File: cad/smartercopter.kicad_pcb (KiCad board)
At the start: 2 copper layers, 37.7 x 16.8 mm, 71 parts, among them P1 CONN_5, P2 CONN_2, P3 CONN_2, P4 CONN_2, Q1 SiA910EDJ, SW1 SW_PUSH_4, U1 CC2541, U2 MPU-9250, U3 TPS73001, U4 TPS73001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

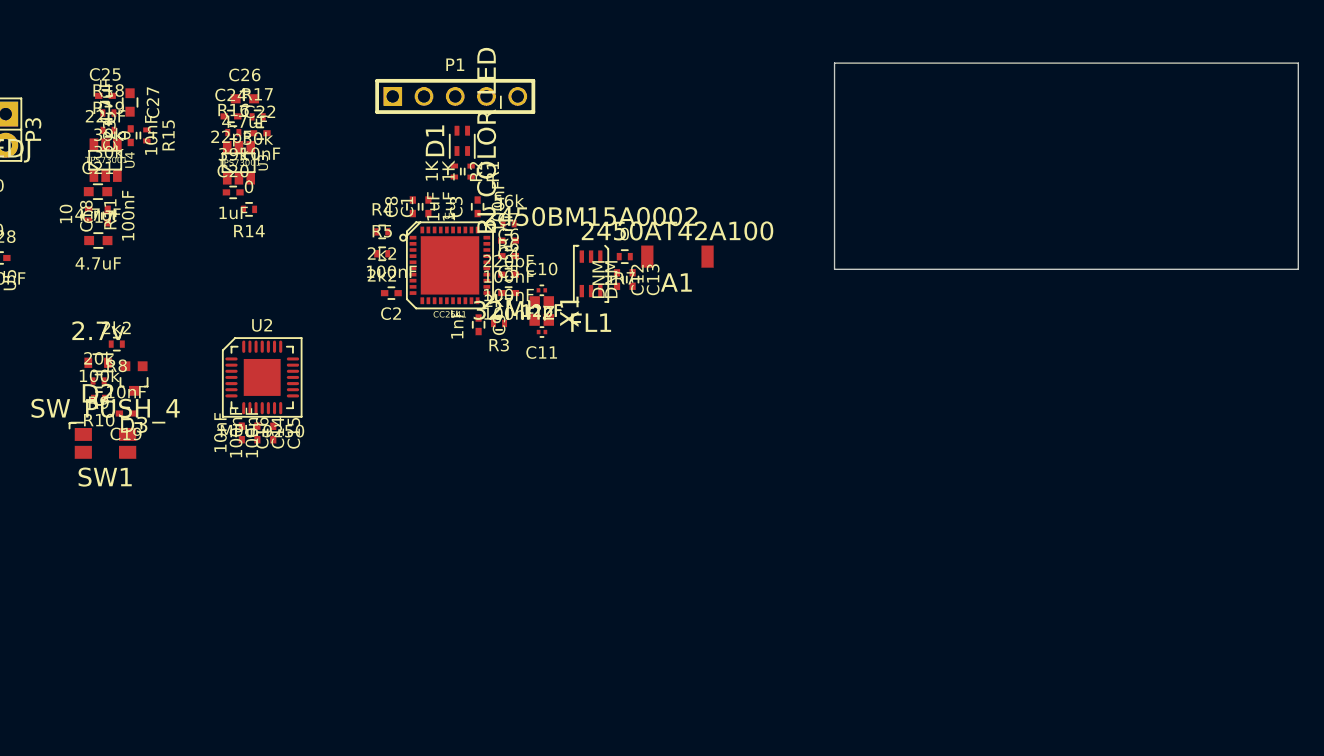
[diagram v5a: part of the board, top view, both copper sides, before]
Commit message: added board outline
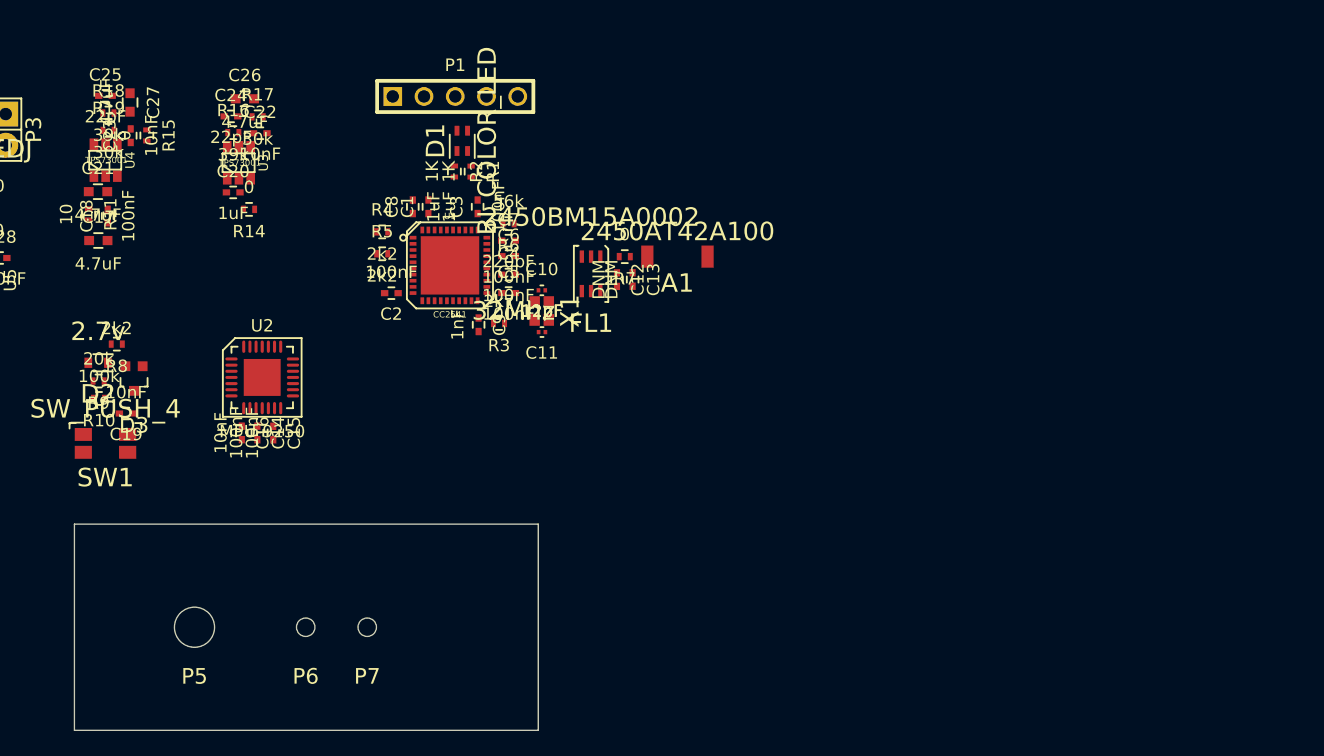
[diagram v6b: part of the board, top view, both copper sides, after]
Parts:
- added P5: CONN_01X01, Mounting_Holes:MountingHole_3mm, F.Cu at (61.1, 112.9)
- added P6: CONN_01X01, Mounting_Holes:MountingHole_3mm, F.Cu at (70.1, 112.9)
- added P7: CONN_01X01, Mounting_Holes:MountingHole_3mm, F.Cu at (75.1, 112.9)
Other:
- board text added: "Receiver"
- board text added: "Wires"
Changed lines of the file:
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@@
     (links 170)
     (no_connects 170)
-    (area 0 0 0 0)
+    (area 113.049999 66.989999 150.850001 83.850001)
     (thickness 1.6)
-    (drawings 4)
+    (drawings 6)
     (tracks 0)
     (zones 0)
-    (modules 71)
+    (modules 74)
     (nets 71)
   )
@@
     (mod_text_width 0.15)
     (pad_size 1.5 1.5)
-    (pad_drill 0.6)
+    (pad_drill 1.5)
     (pad_to_mask_clearance 0)
     (aux_axis_origin 0 0)
-    (visible_elements FFFCFF7F)
+    (visible_elements FFFEFF7F)
     (pcbplotparams
       (layerselection 0x00030_80000001)
@@
       (net 4 DGND))
   )
-  (gr_line (start 150.8 83.8) (end 113.1 83.8) (layer Edge.Cuts) (width 0.1))
-  (gr_line (start 150.8 67.04) (end 150.8 83.8) (layer Edge.Cuts) (width 0.1))
-  (gr_line (start 113.1 67.04) (end 150.8 67.04) (layer Edge.Cuts) (width 0.1))
-  (gr_line (start 113.1 83.8) (end 113.1 67.04) (layer Edge.Cuts) (width 0.1))
+  (module Mounting_Holes:MountingHole_3mm (layer F.Cu)
+    (at 61.075056 112.89367 180)
+    (descr "Mounting hole, Befestigungsbohrung, 3mm, No Annular, Kein Restring,")
+    (tags "Mounting hole, Befestigungsbohrung, 3mm, No Annular, Kein Restring,")
+    (fp_text reference P5 (at 0 -4.0005 180) (layer F.SilkS)
+      (effects (font (thickness 0.3048)))
+    )
+    (fp_text value CONN_01X01 (at 1.00076 5.00126 180) (layer F.SilkS) hide
+      (effects (font (thickness 0.3048)))
+    )
+    (fp_circle (center 0 0) (end 2.99974 0) (layer Cmts.User) (width 0.381))
+    (pad "" np_thru_hole circle (at 0 0 180) (size 3.26 3.26) (drill 3.26) (layers *.Cu *.Mask F.SilkS))
+  )
+  (module Mounting_Holes:MountingHole_3mm (layer F.Cu)
+    (at 70.115056 112.89367 180)
+    (descr "Mounting hole, Befestigungsbohrung, 3mm, No Annular, Kein Restring,")
+    (tags "Mounting hole, Befestigungsbohrung, 3mm, No Annular, Kein Restring,")
+    (fp_text reference P6 (at 0 -4.0005 180) (layer F.SilkS)
+      (effects (font (thickness 0.3048)))
+    )
+    (fp_text value CONN_01X01 (at 1.00076 5.00126 180) (layer F.SilkS) hide
+      (effects (font (thickness 0.3048)))
+    )
+    (fp_circle (center 0 0) (end 2.99974 0) (layer Cmts.User) (width 0.381))
+    (pad "" np_thru_hole circle (at 0 0 180) (size 1.5 1.5) (drill 1.5) (layers *.Cu *.Mask F.SilkS))
+  )
+  (module Mounting_Holes:MountingHole_3mm (layer F.Cu)
+    (at 75.115056 112.89367 180)
+    (descr "Mounting hole, Befestigungsbohrung, 3mm, No Annular, Kein Restring,")
+    (tags "Mounting hole, Befestigungsbohrung, 3mm, No Annular, Kein Restring,")
+    (fp_text reference P7 (at 0 -4.0005 180) (layer F.SilkS)
+      (effects (font (thickness 0.3048)))
+    )
+    (fp_text value CONN_01X01 (at 1.00076 5.00126 180) (layer F.SilkS) hide
+      (effects (font (thickness 0.3048)))
+    )
+    (fp_circle (center 0 0) (end 2.99974 0) (layer Cmts.User) (width 0.381))
+    (pad "" np_thru_hole circle (at 0 0 180) (size 1.5 1.5) (drill 1.5) (layers *.Cu *.Mask F.SilkS))
+  )
+  (gr_text Receiver (at 49.56 112.86 90) (layer Cmts.User)
+    (effects (font (size 1.5 1.5) (thickness 0.3)))
+  )
+  (gr_text Wires (at 90.88 113.06 270) (layer Cmts.User)
+    (effects (font (size 1.5 1.5) (thickness 0.3)))
+  )
+  (gr_line (start 51.315056 104.51367) (end 89.015056 104.51367) (layer Edge.Cuts) (width 0.1))
+  (gr_line (start 51.315056 121.27367) (end 51.315056 104.51367) (layer Edge.Cuts) (width 0.1))
+  (gr_line (start 89.015056 121.27367) (end 51.315056 121.27367) (layer Edge.Cuts) (width 0.1))
+  (gr_line (start 89.015056 104.51367) (end 89.015056 121.27367) (layer Edge.Cuts) (width 0.1))
 )

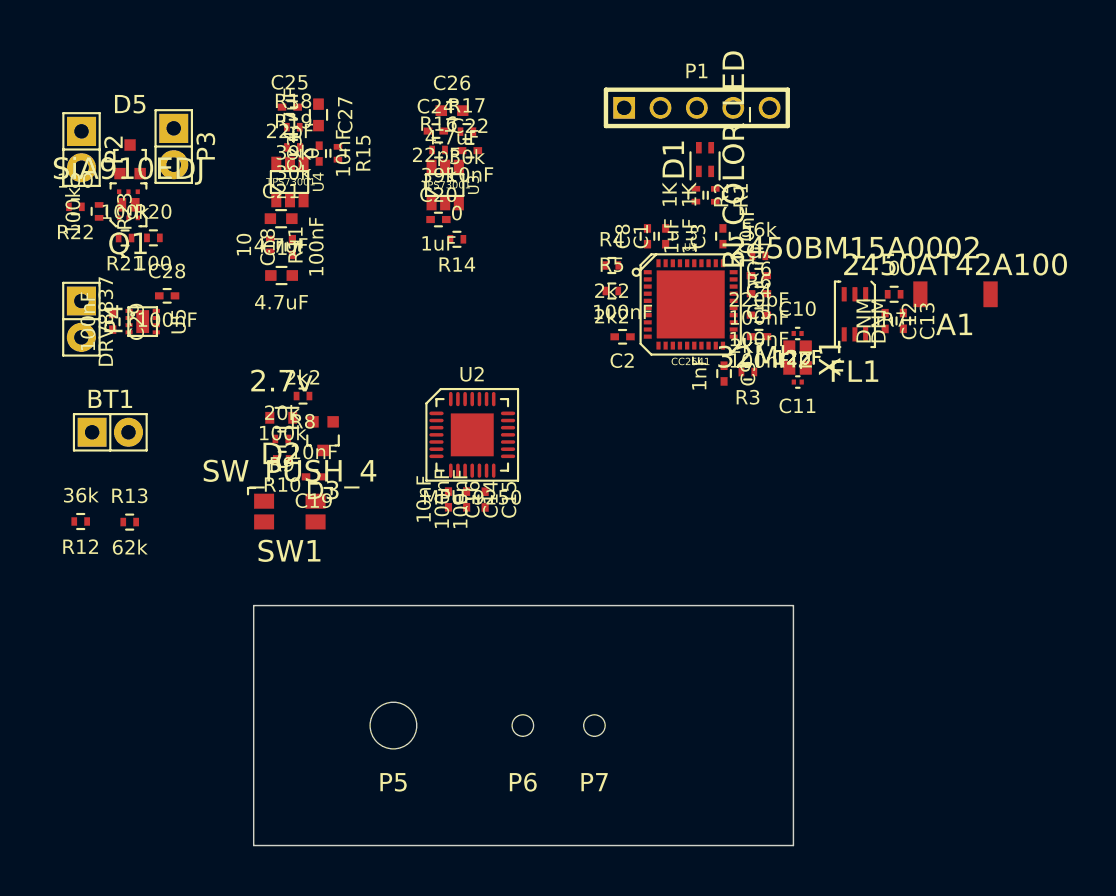
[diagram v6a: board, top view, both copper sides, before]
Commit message: made motor pads single to save space
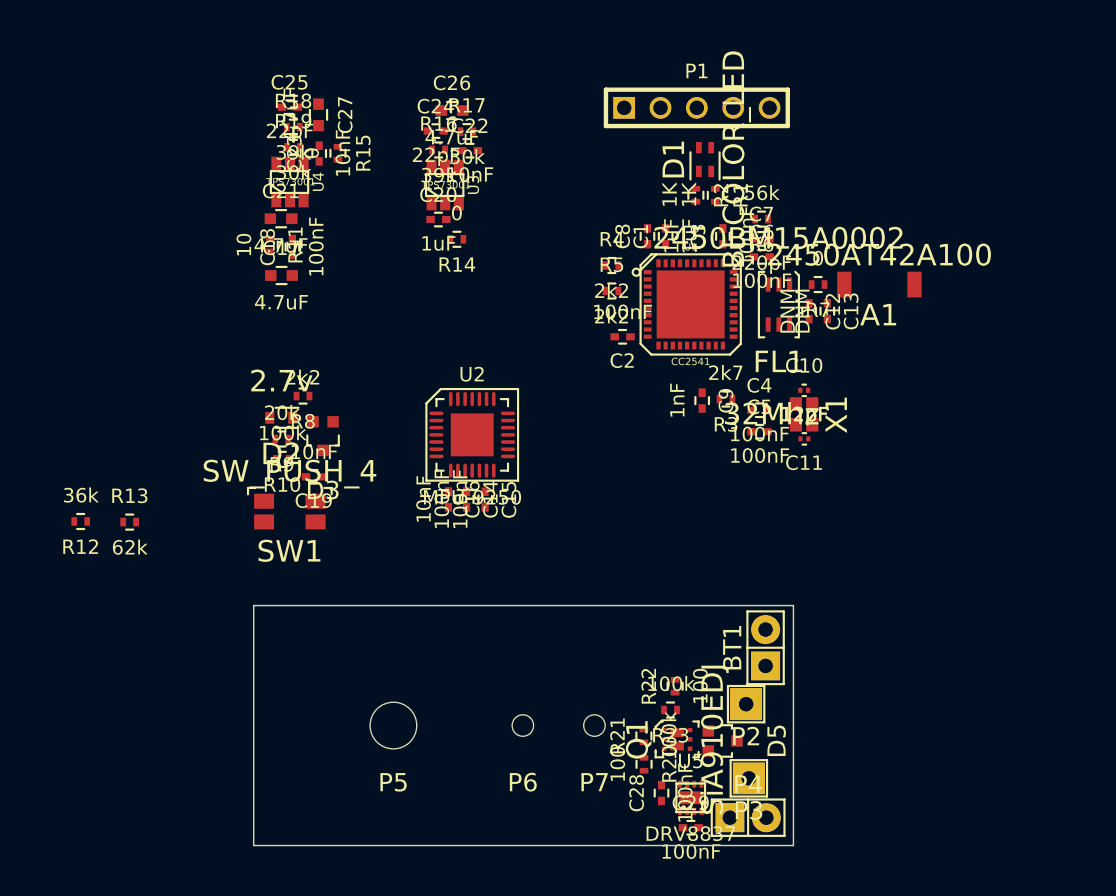
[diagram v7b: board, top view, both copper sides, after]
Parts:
- P2, P3: value CONN_2 -> CONN_01X01; footprint Pin_Headers:Pin_Header_Straight_1x02 -> Pin_Headers:Pin_Header_Straight_1x01
- moved P2 60.5 mm to (85.7, 111.4), turned to 180 degrees
- moved P3 59.7 mm to (85.9, 116.6), turned to 180 degrees
- moved P4 58.1 mm to (85.8, 119.3), turned to 0 degrees
- moved D5 58.0 mm to (84.1, 114.0), turned to 270 degrees
- moved C29 53.7 mm to (81.8, 120.0), turned to 0 degrees
- moved R22 53.6 mm to (80.8, 110.2), turned to 90 degrees
- moved Q1 53.5 mm to (80.9, 113.9), turned to 270 degrees
- moved R23 53.0 mm to (80.4, 111.8), turned to 180 degrees
- moved U5 50.7 mm to (81.8, 117.9), turned to 90 degrees
- moved R20 50.3 mm to (78.6, 115.6), turned to 270 degrees
- moved R21 50.2 mm to (78.6, 113.6), turned to 90 degrees
- moved C28 49.0 mm to (79.8, 117.6), turned to 90 degrees
- moved BT1 48.2 mm to (87.1, 107.5), turned to 90 degrees
- moved C4 6.64 mm to (86.6, 90.9)
- moved C5 6.64 mm to (86.7, 92.4)
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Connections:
- P2 pad 1: +BATT -> Net-(D5-Pad1)
- P3 pad 1: +BATT -> Net-(D5-Pad2)

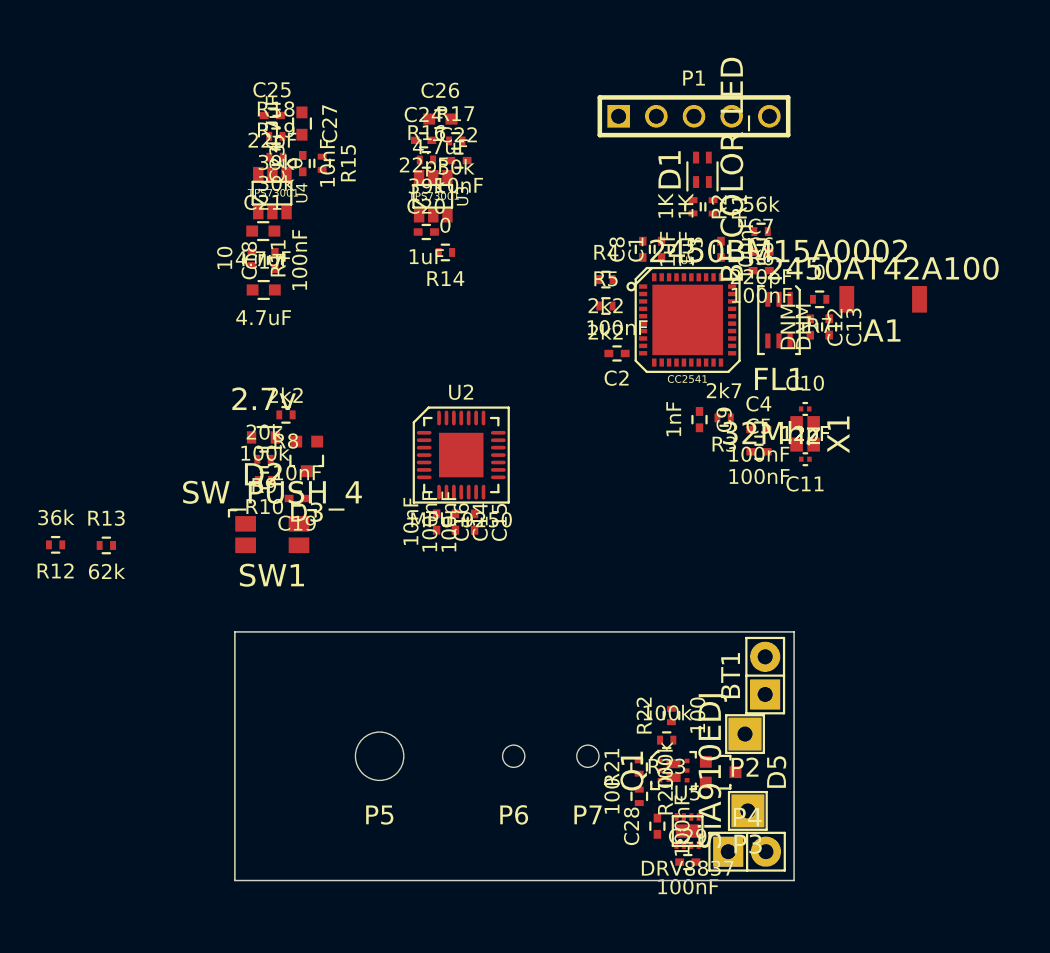
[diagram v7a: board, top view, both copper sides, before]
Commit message: packed most of the components on to board
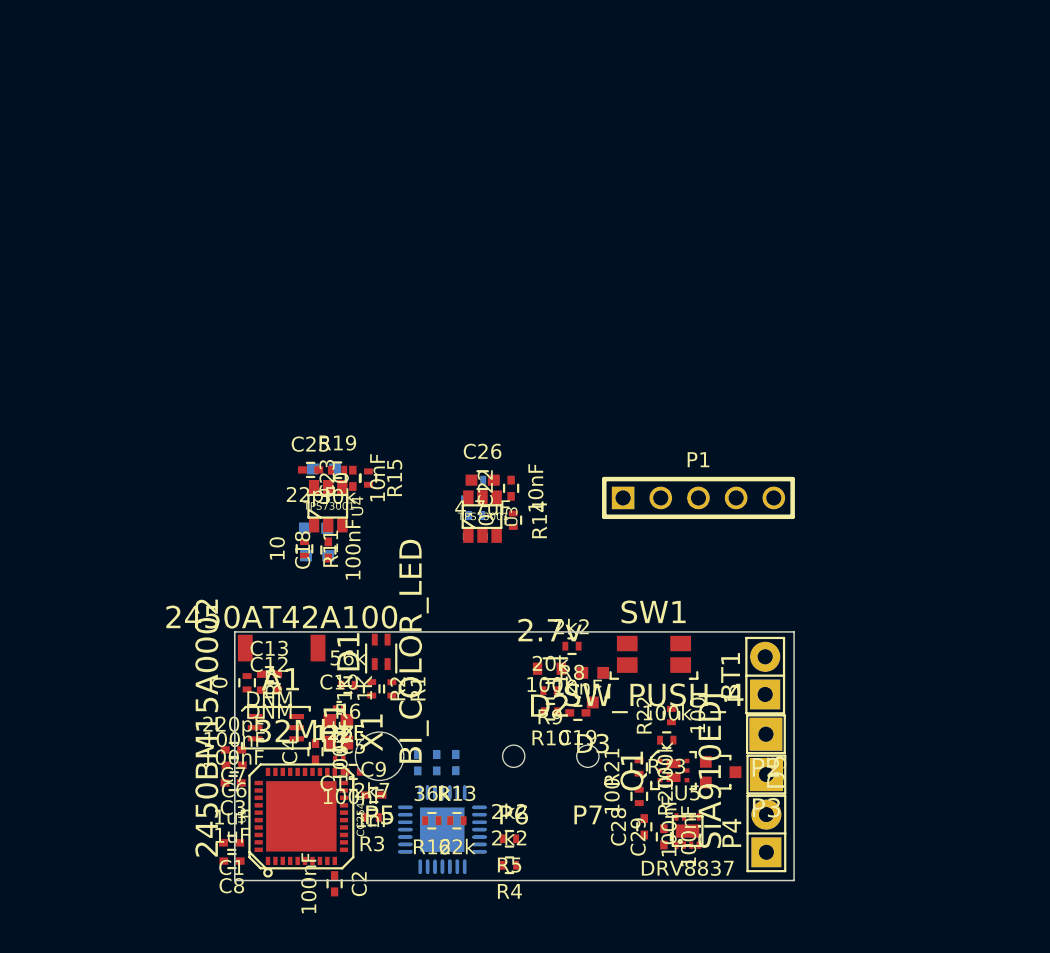
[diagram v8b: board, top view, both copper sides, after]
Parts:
- C14, C15, C16, C17, C20, C21, C24, C27, R16, R17, R18, U2: moved to B.Cu
- moved C8 49.7 mm to (51.1, 120.0), turned to 180 degrees
- moved C1 49.4 mm to (51.1, 118.7), turned to 180 degrees
- moved C7 48.9 mm to (51.2, 112.5), turned to 180 degrees
- moved C3 48.7 mm to (51.2, 114.7), turned to 180 degrees
- moved C6 48.7 mm to (51.3, 113.5), turned to 180 degrees
- moved A1 46.9 mm to (54.5, 105.6)
- moved R7 46.5 mm to (52.1, 107.9), turned to 270 degrees
- moved C13 44.4 mm to (53.6, 107.4), turned to 0 degrees
- moved C12 43.9 mm to (53.6, 108.4), turned to 0 degrees
- moved FL1 43.7 mm to (54.1, 111.0), turned to 90 degrees
- moved U1 42.4 mm to (55.8, 117.0), turned to 90 degrees
- moved R6 41.4 mm to (58.9, 108.1)
- moved C2 40.5 mm to (58.0, 121.5), turned to 270 degrees
- moved R4 40.0 mm to (69.8, 120.2), turned to 180 degrees
- moved D1 39.1 mm to (61.2, 105.9)
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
